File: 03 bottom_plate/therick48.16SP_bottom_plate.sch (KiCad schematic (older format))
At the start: 89 parts, among them U1 HOLE, U10 HOLE, U11 HOLE, U12 HOLE, U13 HOLE, U14 HOLE, U15 HOLE, U16 HOLE, U17 HOLE, U18 HOLE, U19 HOLE, U2 HOLE, U20 HOLE, U21 HOLE, U22 HOLE, U23 HOLE, U24 HOLE, U25 HOLE, U26 HOLE, U27 HOLE, U28 HOLE, U29 HOLE, U3 HOLE, U30 HOLE, U31 HOLE, U32 HOLE, U33 HOLE, U34 HOLE, U35 HOLE, U36 HOLE, U37 HOLE, U38 HOLE, U39 HOLE, U4 HOLE, U40 HOLE, U41 HOLE, U42 HOLE, U43 HOLE, U44 HOLE, U45 HOLE, U46 HOLE, U47 HOLE, U48 HOLE, U49 HOLE, U5 HOLE, U50 HOLE, U51 HOLE, U52 HOLE, U53 HOLE, U54 HOLE, U55 HOLE, U56 HOLE, U57 HOLE, U58 HOLE, U59 HOLE, U6 HOLE, U60 HOLE, U61 HOLE, U62 HOLE, U63 HOLE, U64 HOLE, U65 HOLE, U66 HOLE, U67 HOLE, U68 HOLE, U69 HOLE, U7 HOLE, U70 HOLE, U8 HOLE, U9 HOLE

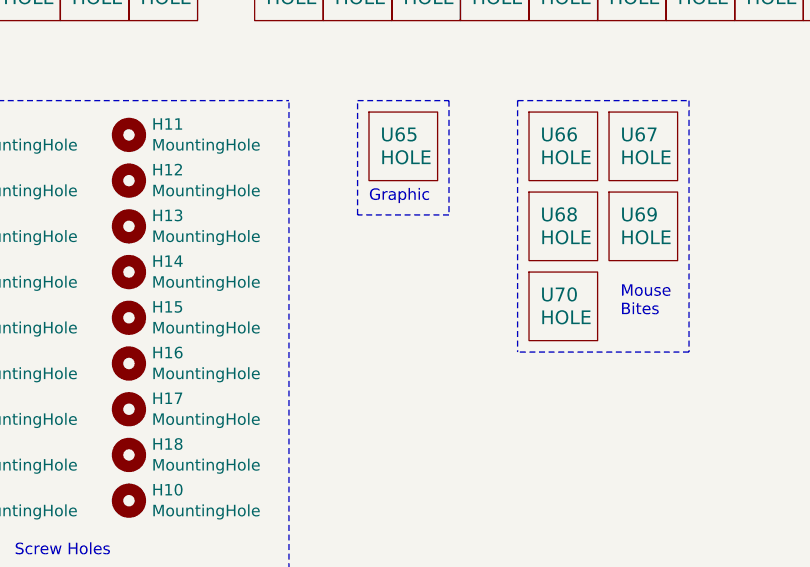
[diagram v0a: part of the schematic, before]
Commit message: Made 2 columns able to be broken away
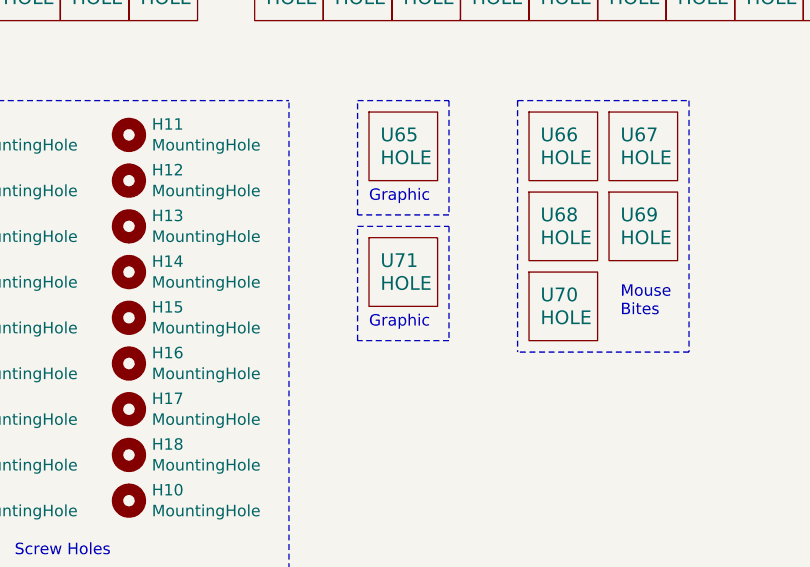
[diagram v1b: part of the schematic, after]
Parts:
- added U71: HOLE, Artwork:THERICK, symbol lets_split-cache:HOLE
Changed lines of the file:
@@
 EESchema Schematic File Version 4
-LIBS:therick64BASP_bottom_plate-cache
+LIBS:therick48.16SP_bottom_plate-cache
 EELAYER 29 0
 EELAYER END
@@
 Wire Notes Line
 	1000 5350 1000 5050
+$Comp
+L lets_split-cache:HOLE U71
+U 1 1 5EDDB181
+P 3150 3700
+F 0 "U71" H 3050 3750 60  0000 L CNN
+F 1 "HOLE" H 3050 3650 60  0000 L CNN
+F 2 "Artwork:THERICK" H 3150 3700 60  0001 C CNN
+F 3 "" H 3150 3700 60  0001 C CNN
+	1    3150 3700
+	1    0    0    -1
+$EndComp
+Text Notes 3000 3950 0    50   ~ 0
+Graphic
+Wire Notes Line
+	2950 4000 2950 3500
+Wire Notes Line
+	2950 3500 3350 3500
+Wire Notes Line
+	3350 3500 3350 4000
+Wire Notes Line
+	3350 4000 2950 4000
 $EndSCHEMATC

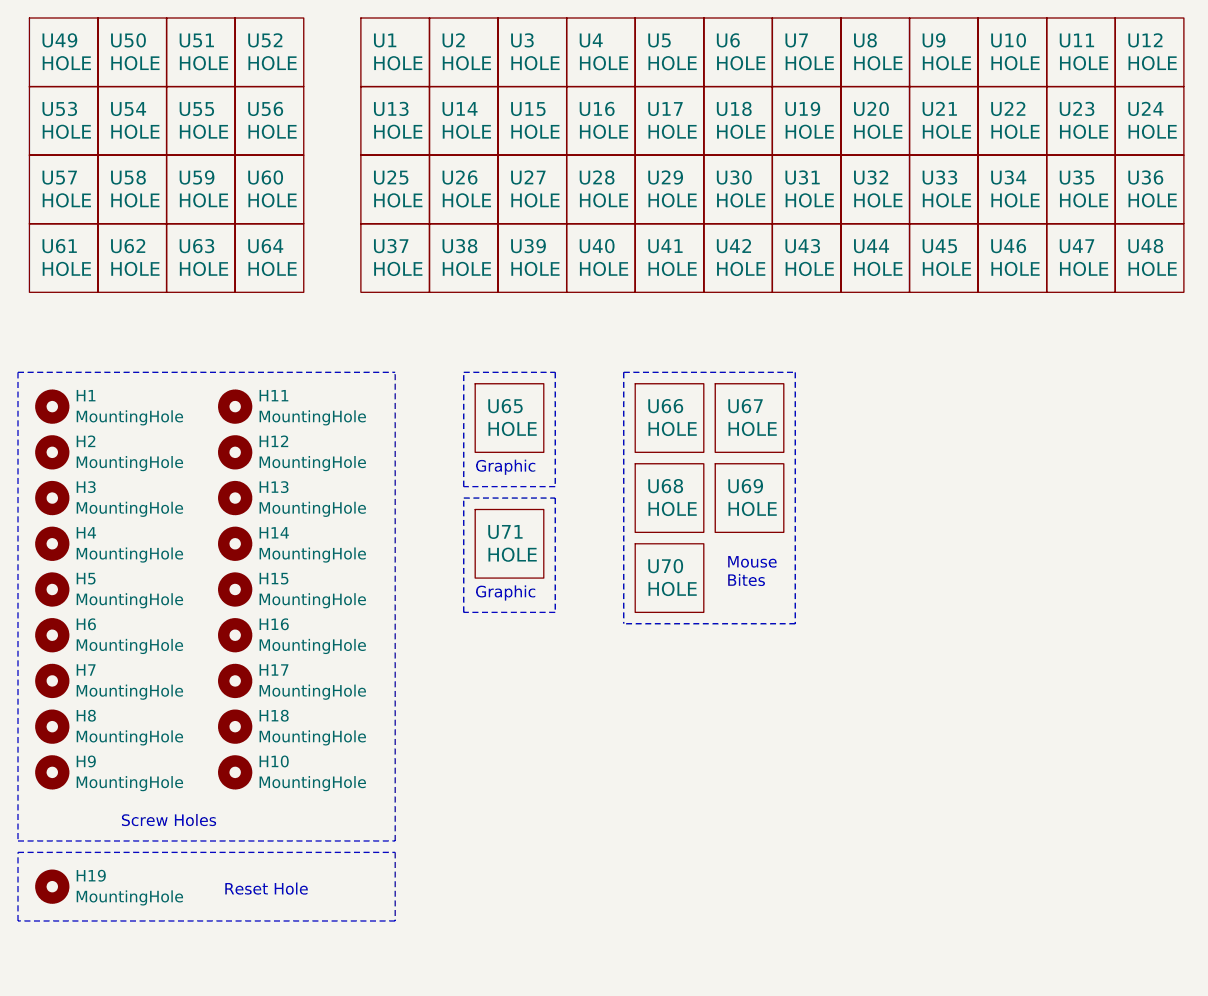
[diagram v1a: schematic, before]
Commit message: Added breakaway section, added rotary encoder support
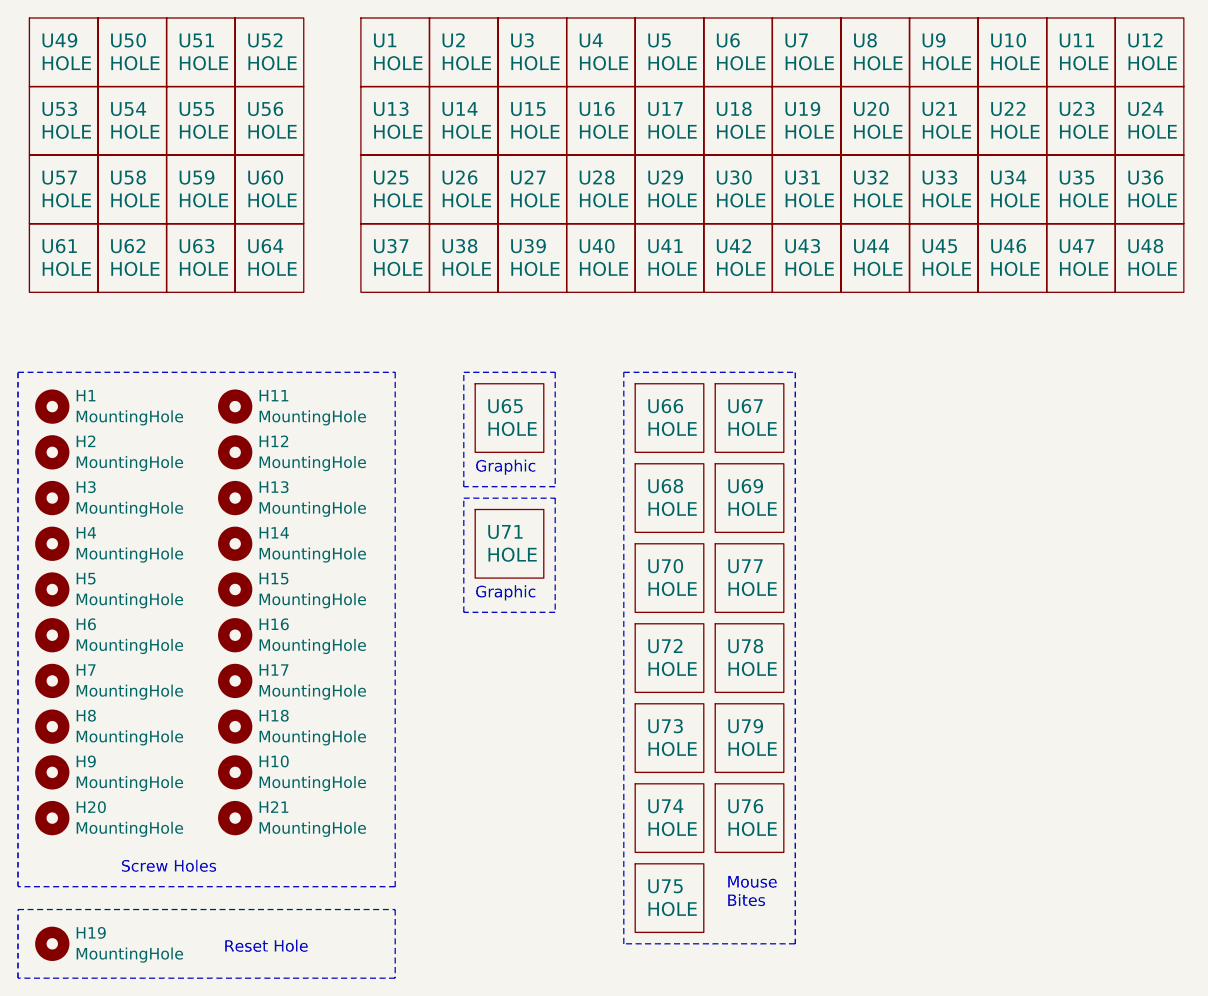
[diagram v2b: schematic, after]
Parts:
- added H20, H21: MountingHole, random-keyboard-parts:Generic-Mounthole, symbol Mechanical:MountingHole
- added U72, U73, U74, U75, U76, U77, U78, U79: HOLE, acheron_Hardware:MouseBite_IPC7351, symbol lets_split-cache:HOLE
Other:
- moved on the sheet: H19
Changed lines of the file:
@@
 	1    0    0    -1
 $EndComp
-Text Notes 1450 4950 0    50   ~ 0
+Text Notes 1450 5150 0    50   ~ 0
 Screw Holes
 Text Notes 3000 3400 0    50   ~ 0
@@
 	1    0    0    -1
 $EndComp
-Text Notes 4100 3900 0    50   ~ 0
-Mouse\nBites
-Wire Notes Line
-	3650 2950 3650 4050
 $Comp
 L lets_split-cache:HOLE U1
@@
 	3650 2950 4400 2950
 Wire Notes Line
-	4400 2950 4400 4050
-Wire Notes Line
-	4400 4050 3650 4050
-Wire Notes Line
 	2950 2950 3350 2950
 Wire Notes Line
@@
 $EndComp
 Wire Notes Line
-	1000 2950 1000 5000
-Wire Notes Line
-	1000 5000 2650 5000
-Wire Notes Line
-	2650 5000 2650 2950
-Wire Notes Line
 	1000 2950 2650 2950
 $Comp
 L Mechanical:MountingHole H19
 U 1 1 5EBF4BCA
-P 1150 5200
-F 0 "H19" H 1250 5246 50  0000 L CNN
-F 1 "MountingHole" H 1250 5155 50  0000 L CNN
-F 2 "random-keyboard-parts:Generic-Mounthole" H 1150 5200 50  0001 C CNN
-F 3 "~" H 1150 5200 50  0001 C CNN
-	1    1150 5200
-	1    0    0    -1
-$EndComp
-Text Notes 1900 5250 0    50   ~ 0
+P 1150 5450
+F 0 "H19" H 1250 5496 50  0000 L CNN
+F 1 "MountingHole" H 1250 5405 50  0000 L CNN
+F 2 "random-keyboard-parts:Generic-Mounthole" H 1150 5450 50  0001 C CNN
+F 3 "~" H 1150 5450 50  0001 C CNN
+	1    1150 5450
+	1    0    0    -1
+$EndComp
+Text Notes 1900 5500 0    50   ~ 0
 Reset Hole
 Wire Notes Line
-	1000 5050 2650 5050
-Wire Notes Line
-	2650 5050 2650 5350
-Wire Notes Line
-	2650 5350 1000 5350
-Wire Notes Line
-	1000 5350 1000 5050
+	1000 5300 2650 5300
+Wire Notes Line
+	2650 5300 2650 5600
+Wire Notes Line
+	2650 5600 1000 5600
+Wire Notes Line
+	1000 5600 1000 5300
 $Comp
 L lets_split-cache:HOLE U71
@@
 Wire Notes Line
 	3350 4000 2950 4000
+$Comp
+L lets_split-cache:HOLE U72
+U 1 1 5EDF35E3
+P 3850 4200
+F 0 "U72" H 3750 4250 60  0000 L CNN
+F 1 "HOLE" H 3750 4150 60  0000 L CNN
+F 2 "acheron_Hardware:MouseBite_IPC7351" H 3850 4200 60  0001 C CNN
+F 3 "" H 3850 4200 60  0001 C CNN
+	1    3850 4200
+	1    0    0    -1
+$EndComp
+$Comp
+L lets_split-cache:HOLE U73
+U 1 1 5EDF35E9
+P 3850 4550
+F 0 "U73" H 3750 4600 60  0000 L CNN
+F 1 "HOLE" H 3750 4500 60  0000 L CNN
+F 2 "acheron_Hardware:MouseBite_IPC7351" H 3850 4550 60  0001 C CNN
+F 3 "" H 3850 4550 60  0001 C CNN
+	1    3850 4550
+	1    0    0    -1
+$EndComp
+$Comp
+L lets_split-cache:HOLE U78
+U 1 1 5EDF35EF
+P 4200 4200
+F 0 "U78" H 4100 4250 60  0000 L CNN
+F 1 "HOLE" H 4100 4150 60  0000 L CNN
+F 2 "acheron_Hardware:MouseBite_IPC7351" H 4200 4200 60  0001 C CNN
+F 3 "" H 4200 4200 60  0001 C CNN
+	1    4200 4200
+	1    0    0    -1
+$EndComp
+$Comp
+L lets_split-cache:HOLE U79
+U 1 1 5EDF35F5
+P 4200 4550
+F 0 "U79" H 4100 4600 60  0000 L CNN
+F 1 "HOLE" H 4100 4500 60  0000 L CNN
+F 2 "acheron_Hardware:MouseBite_IPC7351" H 4200 4550 60  0001 C CNN
+F 3 "" H 4200 4550 60  0001 C CNN
+	1    4200 4550
+	1    0    0    -1
+$EndComp
+$Comp
+L lets_split-cache:HOLE U77
+U 1 1 5EDF35FB
+P 4200 3850
+F 0 "U77" H 4100 3900 60  0000 L CNN
+F 1 "HOLE" H 4100 3800 60  0000 L CNN
+F 2 "acheron_Hardware:MouseBite_IPC7351" H 4200 3850 60  0001 C CNN
+F 3 "" H 4200 3850 60  0001 C CNN
+	1    4200 3850
+	1    0    0    -1
+$EndComp
+$Comp
+L lets_split-cache:HOLE U74
+U 1 1 5EDF458B
+P 3850 4900
+F 0 "U74" H 3750 4950 60  0000 L CNN
+F 1 "HOLE" H 3750 4850 60  0000 L CNN
+F 2 "acheron_Hardware:MouseBite_IPC7351" H 3850 4900 60  0001 C CNN
+F 3 "" H 3850 4900 60  0001 C CNN
+	1    3850 4900
+	1    0    0    -1
+$EndComp
+$Comp
+L lets_split-cache:HOLE U76
+U 1 1 5EDF45A3
+P 4200 4900
+F 0 "U76" H 4100 4950 60  0000 L CNN
+F 1 "HOLE" H 4100 4850 60  0000 L CNN
+F 2 "acheron_Hardware:MouseBite_IPC7351" H 4200 4900 60  0001 C CNN
+F 3 "" H 4200 4900 60  0001 C CNN
+	1    4200 4900
+	1    0    0    -1
+$EndComp
+$Comp
+L Mechanical:MountingHole H20
+U 1 1 5EF2254B
+P 1150 4900
+F 0 "H20" H 1250 4946 50  0000 L CNN
+F 1 "MountingHole" H 1250 4855 50  0000 L CNN
+F 2 "random-keyboard-parts:Generic-Mounthole" H 1150 4900 50  0001 C CNN
+F 3 "~" H 1150 4900 50  0001 C CNN
+	1    1150 4900
+	1    0    0    -1
+$EndComp
+$Comp
+L Mechanical:MountingHole H21
+U 1 1 5EF22551
+P 1950 4900
+F 0 "H21" H 2050 4946 50  0000 L CNN
+F 1 "MountingHole" H 2050 4855 50  0000 L CNN
+F 2 "random-keyboard-parts:Generic-Mounthole" H 1950 4900 50  0001 C CNN
+F 3 "~" H 1950 4900 50  0001 C CNN
+	1    1950 4900
+	1    0    0    -1
+$EndComp
+$Comp
+L lets_split-cache:HOLE U75
+U 1 1 5EDF4591
+P 3850 5250
+F 0 "U75" H 3750 5300 60  0000 L CNN
+F 1 "HOLE" H 3750 5200 60  0000 L CNN
+F 2 "acheron_Hardware:MouseBite_IPC7351" H 3850 5250 60  0001 C CNN
+F 3 "" H 3850 5250 60  0001 C CNN
+	1    3850 5250
+	1    0    0    -1
+$EndComp
+Text Notes 4100 5300 0    50   ~ 0
+Mouse\nBites
+Wire Notes Line
+	4400 2950 4400 5450
+Wire Notes Line
+	4400 5450 3650 5450
+Wire Notes Line
+	3650 5450 3650 2950
+Wire Notes Line
+	2650 5200 1000 5200
+Wire Notes Line
+	1000 2950 1000 5200
+Wire Notes Line
+	2650 2950 2650 5200
 $EndSCHEMATC
